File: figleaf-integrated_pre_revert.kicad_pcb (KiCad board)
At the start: 2 copper layers, 145 x 106 mm, 70 parts, among them J1 Conn_01x02_Pin, J2 HRO_TYPE-C-31-M-14, J3 Battery, J9 TC2030_SWD, Q2 2N7002, SW1 PWR, SW2 RST, U1 SRV05-4, U10 MAX17048, U3 BQ24075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

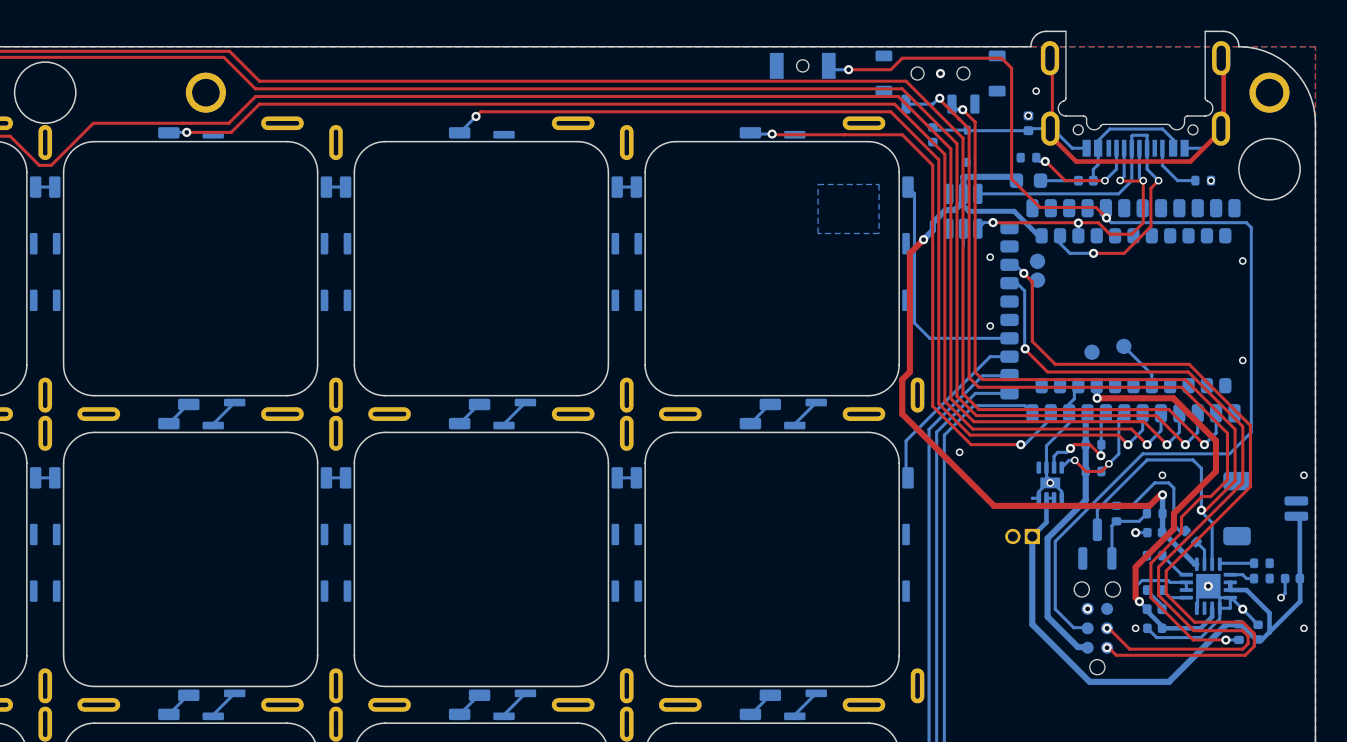
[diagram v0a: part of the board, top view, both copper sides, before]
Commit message: move MCU inwards
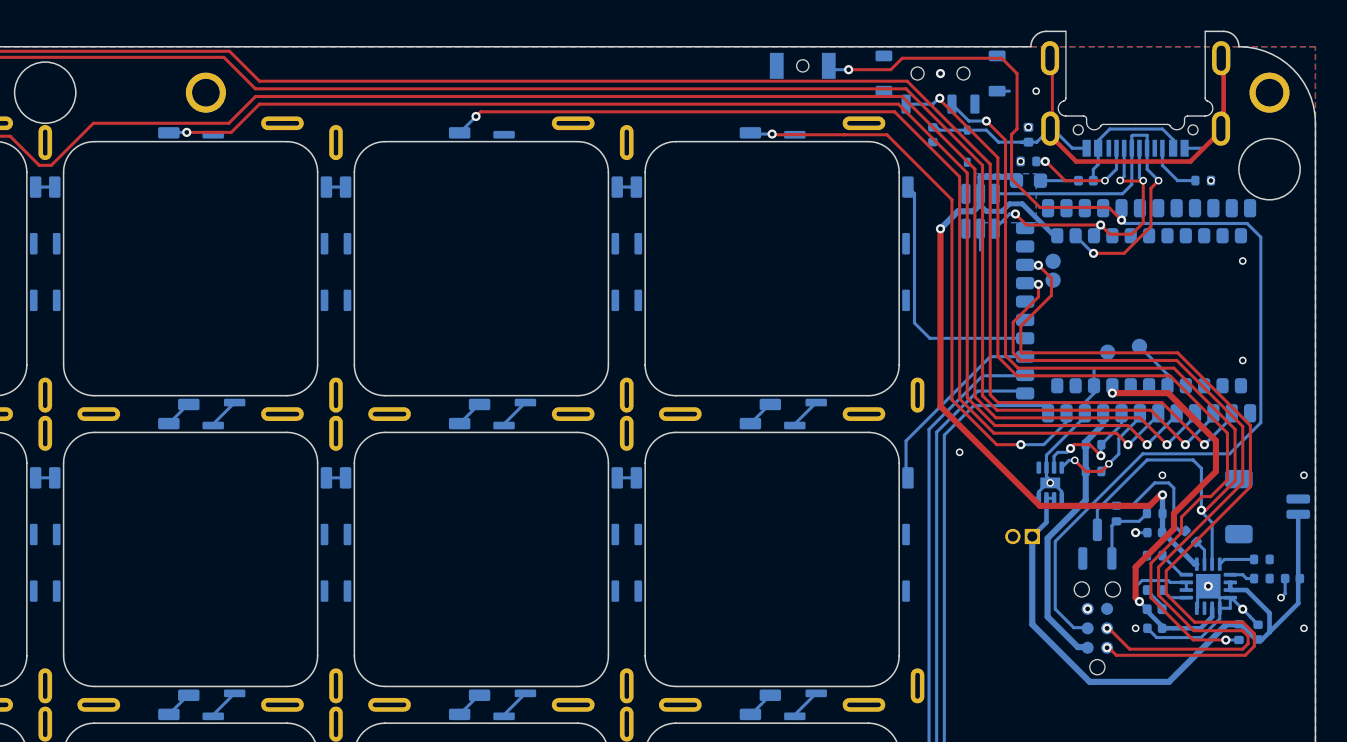
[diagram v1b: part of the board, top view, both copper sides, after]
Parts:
- moved U1 1.11 mm to (135.6, 23.2)
- moved U8 1.02 mm to (148.8, 29.8)
- moved L2 0.75 mm to (138.8, 18.2)
- moved R13 0.25 mm to (154.0, 46.0)
- moved R2 0.25 mm to (138.8, 20.0)
- moved J3 0.18 mm to (154.4, 42.5)
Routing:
- net +5V: track 53.3 -> 48.6 mm
- net GND_L: track 39.4 -> 42.0 mm, vias 20 -> 19
- net SWDIO: track 53.3 -> 55.6 mm
- net USB-D+: track 28.4 -> 26.1 mm
- net Net-(SW1-A): track 59.8 -> 57.9 mm
- net SWDCLK: track 52.1 -> 53.8 mm
- net SYSOFF: track 59.5 -> 58.2 mm
- net +VSW: track 34.1 -> 32.9 mm
- net row_3: track 47.6 -> 48.7 mm
- net Earth: track 37.2 -> 38.3 mm
- net row_2: track 29.5 -> 30.5 mm
- net row_1: track 11.5 -> 12.5 mm
- net row_0: track 15.7 -> 16.7 mm
- net RST: track 73.7 -> 74.6 mm
- net col_0: track 150.0 -> 149.1 mm
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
